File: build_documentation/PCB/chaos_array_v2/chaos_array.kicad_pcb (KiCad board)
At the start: 2 copper layers, 114 x 44 mm, 19 parts, among them SW1 SW_Push, SW2 SW_Push, SW3 OS/Left_Right-hand_Switch, SW4 SW_Push, SW5 SW_Push, U1 RP2040-Zero

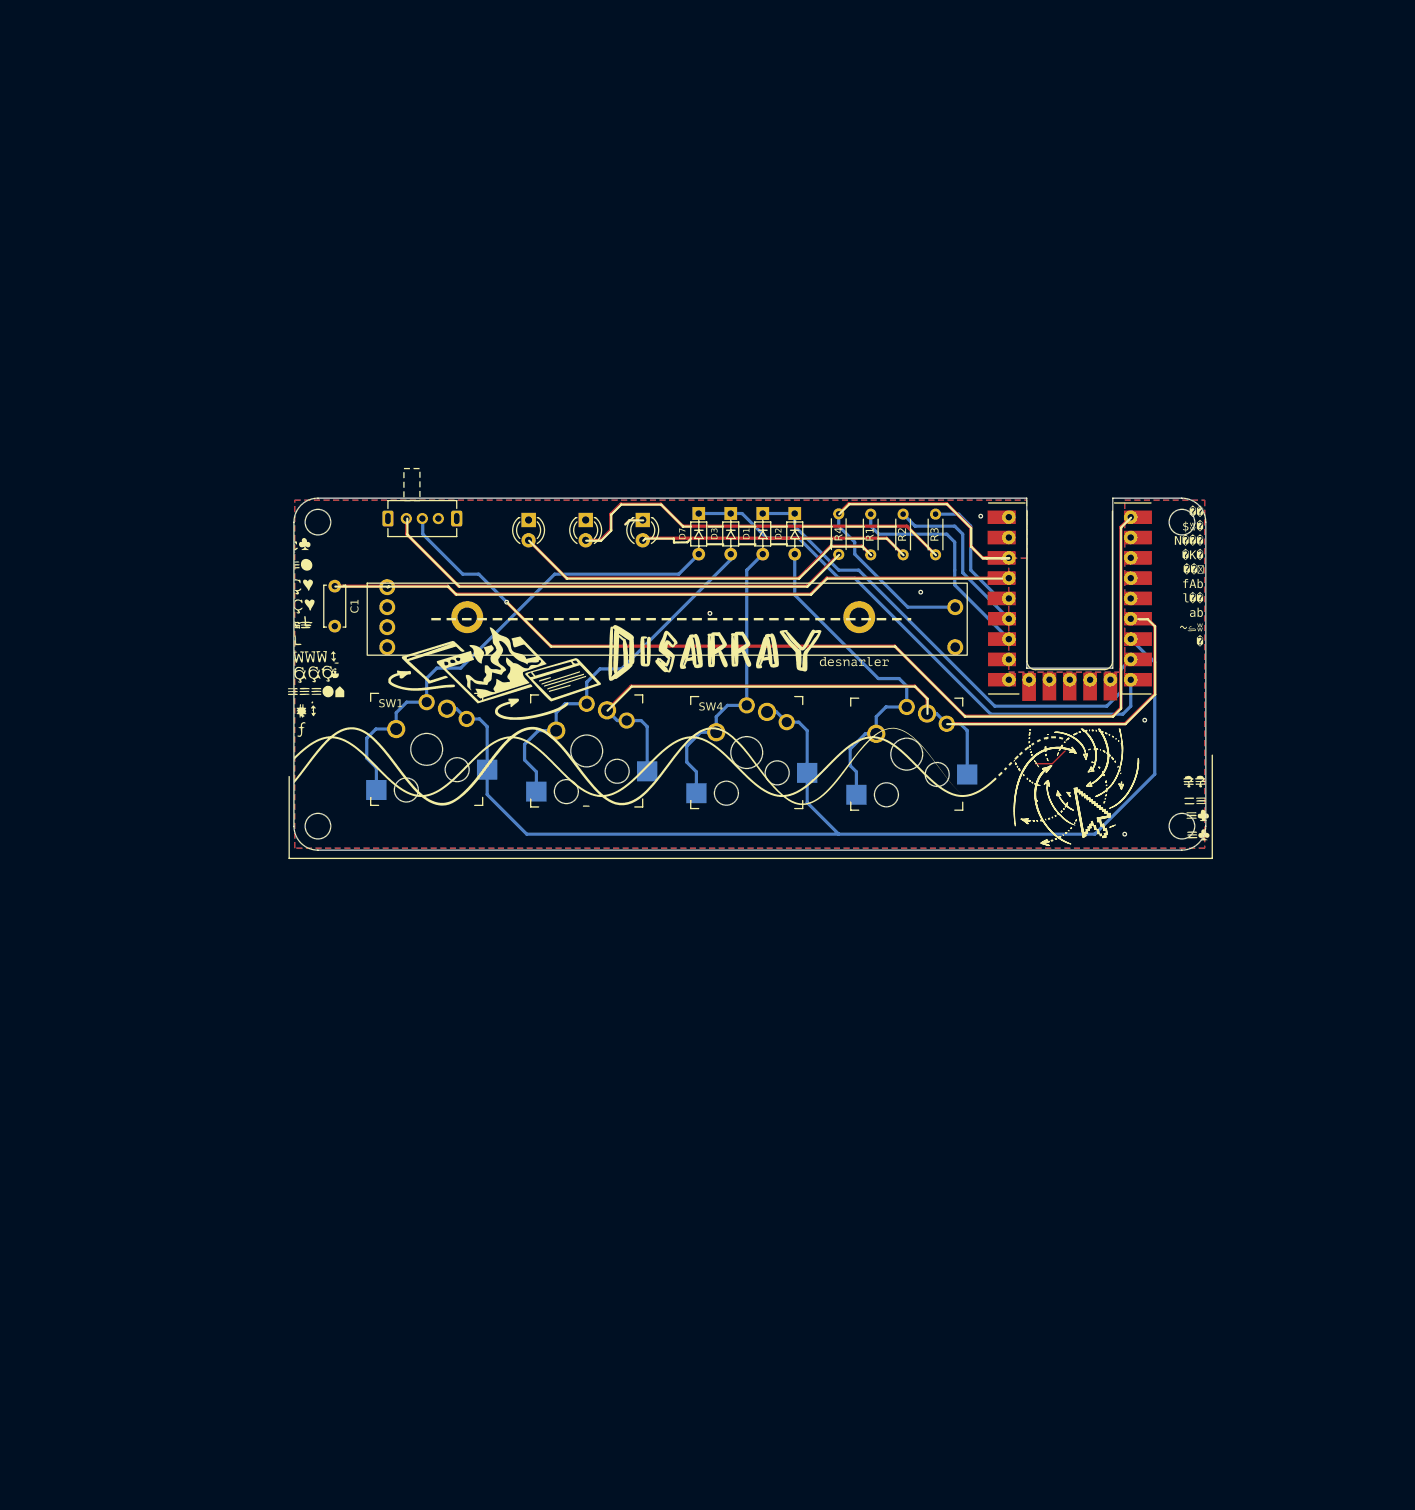
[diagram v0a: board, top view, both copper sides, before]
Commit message: basic layout PCB
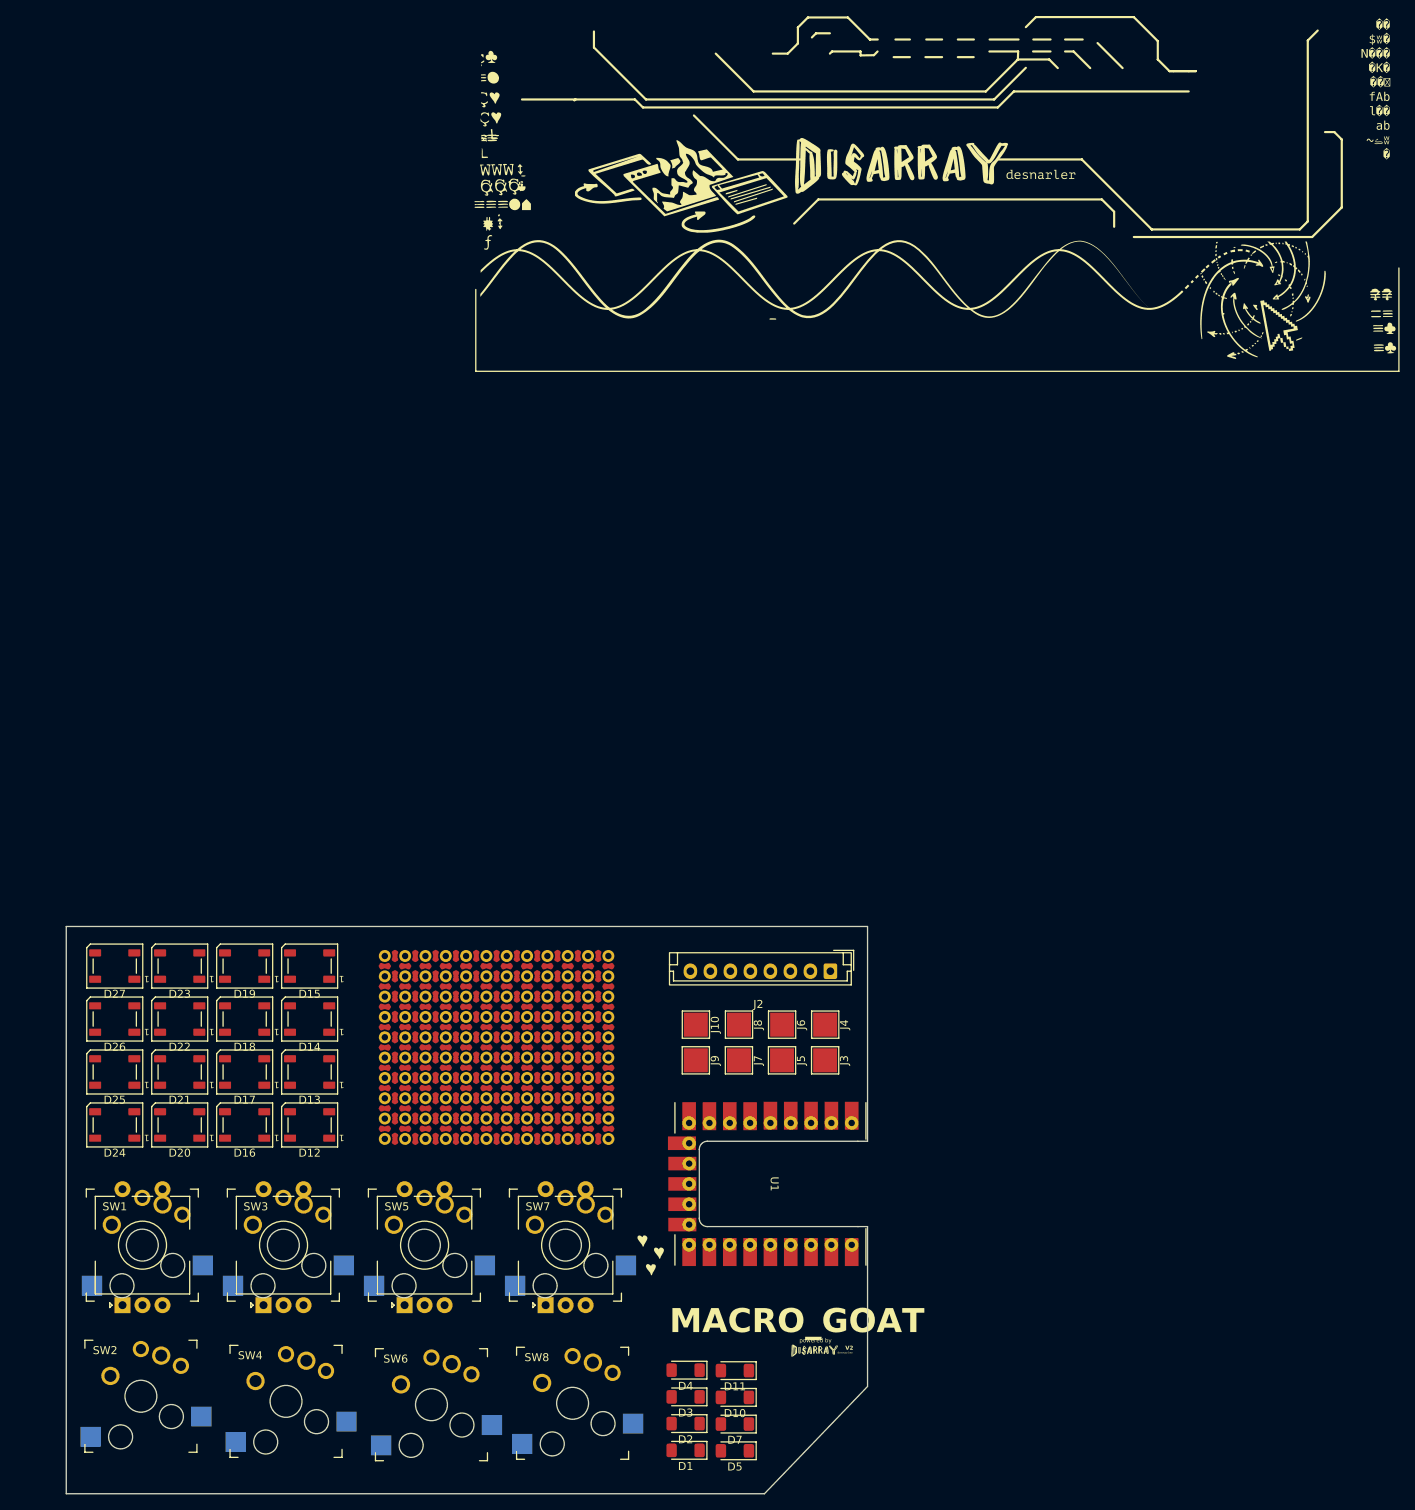
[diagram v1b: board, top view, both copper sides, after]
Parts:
- removed C1: C, Capacitor_THT:C_Disc_D5.0mm_W2.5mm_P5.00mm
- removed D6, D8, D9: LED, LED_THT:LED_D3.0mm
- removed R1, R2, R3: 100R, Resistor_THT:R_Axial_DIN0204_L3.6mm_D1.6mm_P5.08mm_Horizontal
- removed R4: 10k, Resistor_THT:R_Axial_DIN0204_L3.6mm_D1.6mm_P5.08mm_Horizontal
- removed RV1: Analogue_input_slider 10k, CustomFootprints:Potentiometer_slide_75mm_range_60mm_2_sets
- added D10: 1N4148WT, Diode_SMD:D_MiniMELF, F.Cu at (158.0, 150.4)
- added D11: 1N4148WT, Diode_SMD:D_MiniMELF, F.Cu at (158.0, 147.1)
- added D12: WS2812B, LED_SMD:LED_WS2812B_PLCC4_5.0x5.0mm_P3.2mm, F.Cu at (104.9, 116.3)
- added D13: WS2812B, LED_SMD:LED_WS2812B_PLCC4_5.0x5.0mm_P3.2mm, F.Cu at (104.9, 109.7)
- added D14: WS2812B, LED_SMD:LED_WS2812B_PLCC4_5.0x5.0mm_P3.2mm, F.Cu at (104.9, 103.1)
- added D15: WS2812B, LED_SMD:LED_WS2812B_PLCC4_5.0x5.0mm_P3.2mm, F.Cu at (104.9, 96.5)
- added D16: WS2812B, LED_SMD:LED_WS2812B_PLCC4_5.0x5.0mm_P3.2mm, F.Cu at (96.7, 116.3)
- added D17: WS2812B, LED_SMD:LED_WS2812B_PLCC4_5.0x5.0mm_P3.2mm, F.Cu at (96.7, 109.7)
- added D18: WS2812B, LED_SMD:LED_WS2812B_PLCC4_5.0x5.0mm_P3.2mm, F.Cu at (96.7, 103.1)
- added D19: WS2812B, LED_SMD:LED_WS2812B_PLCC4_5.0x5.0mm_P3.2mm, F.Cu at (96.7, 96.5)
- added D20: WS2812B, LED_SMD:LED_WS2812B_PLCC4_5.0x5.0mm_P3.2mm, F.Cu at (88.6, 116.3)
- added D21: WS2812B, LED_SMD:LED_WS2812B_PLCC4_5.0x5.0mm_P3.2mm, F.Cu at (88.6, 109.7)
- added D22: WS2812B, LED_SMD:LED_WS2812B_PLCC4_5.0x5.0mm_P3.2mm, F.Cu at (88.6, 103.1)
- added D23: WS2812B, LED_SMD:LED_WS2812B_PLCC4_5.0x5.0mm_P3.2mm, F.Cu at (88.6, 96.5)
- added D24: WS2812B, LED_SMD:LED_WS2812B_PLCC4_5.0x5.0mm_P3.2mm, F.Cu at (80.5, 116.3)
- added D25: WS2812B, LED_SMD:LED_WS2812B_PLCC4_5.0x5.0mm_P3.2mm, F.Cu at (80.5, 109.7)
- added D26: WS2812B, LED_SMD:LED_WS2812B_PLCC4_5.0x5.0mm_P3.2mm, F.Cu at (80.5, 103.1)
- added D27: WS2812B, LED_SMD:LED_WS2812B_PLCC4_5.0x5.0mm_P3.2mm, F.Cu at (80.5, 96.5)
- added D4: 1N4148WT, Diode_SMD:D_MiniMELF, F.Cu at (151.9, 147.0)
- added D5: 1N4148WT, Diode_SMD:D_MiniMELF, F.Cu at (158.0, 157.1)
- added J10: Conn_01x01_Pin, TestPoint:TestPoint_Pad_3.0x3.0mm, F.Cu at (153.1, 103.8)
- added J2: Conn_01x08_Socket, Connector_JST:JST_EH_B8B-EH-A_1x08_P2.50mm_Vertical, F.Cu at (170.0, 97.1)
- added J3: Conn_01x01_Pin, TestPoint:TestPoint_Pad_3.0x3.0mm, F.Cu at (169.3, 108.3)
- added J4: Conn_01x01_Pin, TestPoint:TestPoint_Pad_3.0x3.0mm, F.Cu at (169.3, 103.8)
- added J5: Conn_01x01_Pin, TestPoint:TestPoint_Pad_3.0x3.0mm, F.Cu at (163.9, 108.3)
- added J6: Conn_01x01_Pin, TestPoint:TestPoint_Pad_3.0x3.0mm, F.Cu at (163.9, 103.8)
- added J7: Conn_01x01_Pin, TestPoint:TestPoint_Pad_3.0x3.0mm, F.Cu at (158.5, 108.3)
- added J8: Conn_01x01_Pin, TestPoint:TestPoint_Pad_3.0x3.0mm, F.Cu at (158.5, 103.8)
- added J9: Conn_01x01_Pin, TestPoint:TestPoint_Pad_3.0x3.0mm, F.Cu at (153.1, 108.3)
- added REF**: PerfBoard_THT_SMD_PAD_BOTTOM, TestPoint:PerfBoard_THT_SMD_PAD_BOTTOM, F.Cu at (142.2, 95.2)
- added REF**: PerfBoard_THT_SMD_PAD_RIGHT, TestPoint:PerfBoard_THT_SMD_PAD_RIGHT, F.Cu at (134.6, 118.1)
- added REF**: PerfBoard_THT_SMD_PAD_BOTTOM, TestPoint:PerfBoard_THT_SMD_PAD_BOTTOM, F.Cu at (142.2, 105.4)
- added REF**: PerfBoard_THT_SMD_PAD_RIGHT, TestPoint:PerfBoard_THT_SMD_PAD_RIGHT, F.Cu at (139.7, 118.1)
- added REF**: PerfBoard_THT_SMD_PAD_BOTTOM, TestPoint:PerfBoard_THT_SMD_PAD_BOTTOM, F.Cu at (142.2, 102.9)
- added REF**: PerfBoard_THT_SMD_PAD_RIGHT, TestPoint:PerfBoard_THT_SMD_PAD_RIGHT, F.Cu at (119.3, 118.1)
- added REF**: PerfBoard_THT_SMD_PAD_BOTTOM, TestPoint:PerfBoard_THT_SMD_PAD_BOTTOM, F.Cu at (142.2, 113.0)
- added REF**: PerfBoard_THT_SMD_PAD_RIGHT, TestPoint:PerfBoard_THT_SMD_PAD_RIGHT, F.Cu at (132.0, 118.1)
- added REF**: PerfBoard_THT_SMD_PAD_BOTTOM, TestPoint:PerfBoard_THT_SMD_PAD_BOTTOM, F.Cu at (142.2, 115.6)
- added REF**: PerfBoard_THT_SMD_PAD_BOTTOM, TestPoint:PerfBoard_THT_SMD_PAD_BOTTOM, F.Cu at (142.2, 97.8)
- added REF**: PerfBoard_THT_SMD_PAD_BOTTOM, TestPoint:PerfBoard_THT_SMD_PAD_BOTTOM, F.Cu at (142.2, 100.3)
- added REF**: PerfBoard_THT_PAD, TestPoint:PerfBoard_THT_PAD, F.Cu at (142.2, 118.1)
- added REF**: PerfBoard_THT_SMD_PAD_RIGHT, TestPoint:PerfBoard_THT_SMD_PAD_RIGHT, F.Cu at (129.5, 118.1)
- added REF**: PerfBoard_THT_SMD_PAD_RIGHT, TestPoint:PerfBoard_THT_SMD_PAD_RIGHT, F.Cu at (116.8, 118.1)
- added REF**: PerfBoard_THT_SMD_PAD_RIGHT, TestPoint:PerfBoard_THT_SMD_PAD_RIGHT, F.Cu at (124.4, 118.1)
- added REF**: PerfBoard_THT_SMD_PAD_RIGHT, TestPoint:PerfBoard_THT_SMD_PAD_RIGHT, F.Cu at (114.3, 118.1)
- added REF**: PerfBoard_THT_SMD_PAD_BOTTOM, TestPoint:PerfBoard_THT_SMD_PAD_BOTTOM, F.Cu at (142.2, 107.9)
- added REF**: PerfBoard_THT_SMD_PAD_BOTTOM, TestPoint:PerfBoard_THT_SMD_PAD_BOTTOM, F.Cu at (142.2, 110.5)
- added REF**: PerfBoard_THT_SMD_PAD_RIGHT, TestPoint:PerfBoard_THT_SMD_PAD_RIGHT, F.Cu at (127.0, 118.1)
- added REF**: PerfBoard_THT_SMD_PAD_RIGHT, TestPoint:PerfBoard_THT_SMD_PAD_RIGHT, F.Cu at (121.9, 118.1)
- added REF**: PerfBoard_THT_SMD_PAD_RIGHT, TestPoint:PerfBoard_THT_SMD_PAD_RIGHT, F.Cu at (137.1, 118.1)
- added REF**100: PerfBoard_THT_SMD_PAD, TestPoint:PerfBoard_THT_SMD_PAD, F.Cu at (116.8, 113.0)
- added REF**101: PerfBoard_THT_SMD_PAD, TestPoint:PerfBoard_THT_SMD_PAD, F.Cu at (119.3, 113.0)
- added REF**102: PerfBoard_THT_SMD_PAD, TestPoint:PerfBoard_THT_SMD_PAD, F.Cu at (121.9, 113.0)
- added REF**103: PerfBoard_THT_SMD_PAD, TestPoint:PerfBoard_THT_SMD_PAD, F.Cu at (124.4, 113.0)
- added REF**104: PerfBoard_THT_SMD_PAD, TestPoint:PerfBoard_THT_SMD_PAD, F.Cu at (127.0, 113.0)
- added REF**105: PerfBoard_THT_SMD_PAD, TestPoint:PerfBoard_THT_SMD_PAD, F.Cu at (129.5, 113.0)
- added REF**106: PerfBoard_THT_SMD_PAD, TestPoint:PerfBoard_THT_SMD_PAD, F.Cu at (132.0, 113.0)
- added REF**107: PerfBoard_THT_SMD_PAD, TestPoint:PerfBoard_THT_SMD_PAD, F.Cu at (134.6, 113.0)
- added REF**108: PerfBoard_THT_SMD_PAD, TestPoint:PerfBoard_THT_SMD_PAD, F.Cu at (137.1, 113.0)
- added REF**109: PerfBoard_THT_SMD_PAD, TestPoint:PerfBoard_THT_SMD_PAD, F.Cu at (139.7, 113.0)
- added REF**110: PerfBoard_THT_SMD_PAD, TestPoint:PerfBoard_THT_SMD_PAD, F.Cu at (114.3, 115.5)
- added REF**111: PerfBoard_THT_SMD_PAD, TestPoint:PerfBoard_THT_SMD_PAD, F.Cu at (116.8, 115.5)
- added REF**112: PerfBoard_THT_SMD_PAD, TestPoint:PerfBoard_THT_SMD_PAD, F.Cu at (119.3, 115.5)
- added REF**113: PerfBoard_THT_SMD_PAD, TestPoint:PerfBoard_THT_SMD_PAD, F.Cu at (121.9, 115.5)
- added REF**114: PerfBoard_THT_SMD_PAD, TestPoint:PerfBoard_THT_SMD_PAD, F.Cu at (124.4, 115.5)
- added REF**115: PerfBoard_THT_SMD_PAD, TestPoint:PerfBoard_THT_SMD_PAD, F.Cu at (127.0, 115.5)
- added REF**116: PerfBoard_THT_SMD_PAD, TestPoint:PerfBoard_THT_SMD_PAD, F.Cu at (129.5, 115.5)
- added REF**117: PerfBoard_THT_SMD_PAD, TestPoint:PerfBoard_THT_SMD_PAD, F.Cu at (132.0, 115.5)
- added REF**118: PerfBoard_THT_SMD_PAD, TestPoint:PerfBoard_THT_SMD_PAD, F.Cu at (134.6, 115.5)
- added REF**119: PerfBoard_THT_SMD_PAD, TestPoint:PerfBoard_THT_SMD_PAD, F.Cu at (137.1, 115.5)
- added REF**120: PerfBoard_THT_SMD_PAD, TestPoint:PerfBoard_THT_SMD_PAD, F.Cu at (139.7, 115.5)
- added REF**22: PerfBoard_THT_SMD_PAD, TestPoint:PerfBoard_THT_SMD_PAD, F.Cu at (114.3, 95.2)
- added REF**23: PerfBoard_THT_SMD_PAD, TestPoint:PerfBoard_THT_SMD_PAD, F.Cu at (116.8, 95.2)
- added REF**24: PerfBoard_THT_SMD_PAD, TestPoint:PerfBoard_THT_SMD_PAD, F.Cu at (119.3, 95.2)
- added REF**25: PerfBoard_THT_SMD_PAD, TestPoint:PerfBoard_THT_SMD_PAD, F.Cu at (121.9, 95.2)
- added REF**26: PerfBoard_THT_SMD_PAD, TestPoint:PerfBoard_THT_SMD_PAD, F.Cu at (124.4, 95.2)
- added REF**27: PerfBoard_THT_SMD_PAD, TestPoint:PerfBoard_THT_SMD_PAD, F.Cu at (127.0, 95.2)
- added REF**28: PerfBoard_THT_SMD_PAD, TestPoint:PerfBoard_THT_SMD_PAD, F.Cu at (129.5, 95.2)
- added REF**29: PerfBoard_THT_SMD_PAD, TestPoint:PerfBoard_THT_SMD_PAD, F.Cu at (132.0, 95.2)
- added REF**30: PerfBoard_THT_SMD_PAD, TestPoint:PerfBoard_THT_SMD_PAD, F.Cu at (134.6, 95.2)
- added REF**31: PerfBoard_THT_SMD_PAD, TestPoint:PerfBoard_THT_SMD_PAD, F.Cu at (137.1, 95.2)
- added REF**32: PerfBoard_THT_SMD_PAD, TestPoint:PerfBoard_THT_SMD_PAD, F.Cu at (139.7, 95.2)
- added REF**33: PerfBoard_THT_SMD_PAD, TestPoint:PerfBoard_THT_SMD_PAD, F.Cu at (114.3, 97.8)
- added REF**34: PerfBoard_THT_SMD_PAD, TestPoint:PerfBoard_THT_SMD_PAD, F.Cu at (116.8, 97.8)
- added REF**35: PerfBoard_THT_SMD_PAD, TestPoint:PerfBoard_THT_SMD_PAD, F.Cu at (119.3, 97.8)
- added REF**36: PerfBoard_THT_SMD_PAD, TestPoint:PerfBoard_THT_SMD_PAD, F.Cu at (121.9, 97.8)
- added REF**37: PerfBoard_THT_SMD_PAD, TestPoint:PerfBoard_THT_SMD_PAD, F.Cu at (124.4, 97.8)
- added REF**38: PerfBoard_THT_SMD_PAD, TestPoint:PerfBoard_THT_SMD_PAD, F.Cu at (127.0, 97.8)
- added REF**39: PerfBoard_THT_SMD_PAD, TestPoint:PerfBoard_THT_SMD_PAD, F.Cu at (129.5, 97.8)
- added REF**40: PerfBoard_THT_SMD_PAD, TestPoint:PerfBoard_THT_SMD_PAD, F.Cu at (132.0, 97.8)
- added REF**41: PerfBoard_THT_SMD_PAD, TestPoint:PerfBoard_THT_SMD_PAD, F.Cu at (134.6, 97.8)
- added REF**42: PerfBoard_THT_SMD_PAD, TestPoint:PerfBoard_THT_SMD_PAD, F.Cu at (137.1, 97.8)
- added REF**43: PerfBoard_THT_SMD_PAD, TestPoint:PerfBoard_THT_SMD_PAD, F.Cu at (139.7, 97.8)
- added REF**44: PerfBoard_THT_SMD_PAD, TestPoint:PerfBoard_THT_SMD_PAD, F.Cu at (114.3, 100.3)
- added REF**45: PerfBoard_THT_SMD_PAD, TestPoint:PerfBoard_THT_SMD_PAD, F.Cu at (116.8, 100.3)
- added REF**46: PerfBoard_THT_SMD_PAD, TestPoint:PerfBoard_THT_SMD_PAD, F.Cu at (119.3, 100.3)
- added REF**47: PerfBoard_THT_SMD_PAD, TestPoint:PerfBoard_THT_SMD_PAD, F.Cu at (121.9, 100.3)
- added REF**48: PerfBoard_THT_SMD_PAD, TestPoint:PerfBoard_THT_SMD_PAD, F.Cu at (124.4, 100.3)
- added REF**49: PerfBoard_THT_SMD_PAD, TestPoint:PerfBoard_THT_SMD_PAD, F.Cu at (127.0, 100.3)
- added REF**50: PerfBoard_THT_SMD_PAD, TestPoint:PerfBoard_THT_SMD_PAD, F.Cu at (129.5, 100.3)
- added REF**51: PerfBoard_THT_SMD_PAD, TestPoint:PerfBoard_THT_SMD_PAD, F.Cu at (132.0, 100.3)
- added REF**52: PerfBoard_THT_SMD_PAD, TestPoint:PerfBoard_THT_SMD_PAD, F.Cu at (134.6, 100.3)
- added REF**53: PerfBoard_THT_SMD_PAD, TestPoint:PerfBoard_THT_SMD_PAD, F.Cu at (137.1, 100.3)
- added REF**54: PerfBoard_THT_SMD_PAD, TestPoint:PerfBoard_THT_SMD_PAD, F.Cu at (139.7, 100.3)
- added REF**55: PerfBoard_THT_SMD_PAD, TestPoint:PerfBoard_THT_SMD_PAD, F.Cu at (114.3, 102.8)
- added REF**56: PerfBoard_THT_SMD_PAD, TestPoint:PerfBoard_THT_SMD_PAD, F.Cu at (116.8, 102.8)
- added REF**57: PerfBoard_THT_SMD_PAD, TestPoint:PerfBoard_THT_SMD_PAD, F.Cu at (119.3, 102.8)
- added REF**58: PerfBoard_THT_SMD_PAD, TestPoint:PerfBoard_THT_SMD_PAD, F.Cu at (121.9, 102.8)
- added REF**59: PerfBoard_THT_SMD_PAD, TestPoint:PerfBoard_THT_SMD_PAD, F.Cu at (124.4, 102.8)
- added REF**60: PerfBoard_THT_SMD_PAD, TestPoint:PerfBoard_THT_SMD_PAD, F.Cu at (127.0, 102.8)
- added REF**61: PerfBoard_THT_SMD_PAD, TestPoint:PerfBoard_THT_SMD_PAD, F.Cu at (129.5, 102.8)
- added REF**62: PerfBoard_THT_SMD_PAD, TestPoint:PerfBoard_THT_SMD_PAD, F.Cu at (132.0, 102.8)
- added REF**63: PerfBoard_THT_SMD_PAD, TestPoint:PerfBoard_THT_SMD_PAD, F.Cu at (134.6, 102.8)
- added REF**64: PerfBoard_THT_SMD_PAD, TestPoint:PerfBoard_THT_SMD_PAD, F.Cu at (137.1, 102.8)
- added REF**65: PerfBoard_THT_SMD_PAD, TestPoint:PerfBoard_THT_SMD_PAD, F.Cu at (139.7, 102.8)
- added REF**66: PerfBoard_THT_SMD_PAD, TestPoint:PerfBoard_THT_SMD_PAD, F.Cu at (114.3, 105.4)
- added REF**67: PerfBoard_THT_SMD_PAD, TestPoint:PerfBoard_THT_SMD_PAD, F.Cu at (116.8, 105.4)
- added REF**68: PerfBoard_THT_SMD_PAD, TestPoint:PerfBoard_THT_SMD_PAD, F.Cu at (119.3, 105.4)
- added REF**69: PerfBoard_THT_SMD_PAD, TestPoint:PerfBoard_THT_SMD_PAD, F.Cu at (121.9, 105.4)
- added REF**70: PerfBoard_THT_SMD_PAD, TestPoint:PerfBoard_THT_SMD_PAD, F.Cu at (124.4, 105.4)
- added REF**71: PerfBoard_THT_SMD_PAD, TestPoint:PerfBoard_THT_SMD_PAD, F.Cu at (127.0, 105.4)
- added REF**72: PerfBoard_THT_SMD_PAD, TestPoint:PerfBoard_THT_SMD_PAD, F.Cu at (129.5, 105.4)
- added REF**73: PerfBoard_THT_SMD_PAD, TestPoint:PerfBoard_THT_SMD_PAD, F.Cu at (132.0, 105.4)
- added REF**74: PerfBoard_THT_SMD_PAD, TestPoint:PerfBoard_THT_SMD_PAD, F.Cu at (134.6, 105.4)
- added REF**75: PerfBoard_THT_SMD_PAD, TestPoint:PerfBoard_THT_SMD_PAD, F.Cu at (137.1, 105.4)
- added REF**76: PerfBoard_THT_SMD_PAD, TestPoint:PerfBoard_THT_SMD_PAD, F.Cu at (139.7, 105.4)
- added REF**77: PerfBoard_THT_SMD_PAD, TestPoint:PerfBoard_THT_SMD_PAD, F.Cu at (114.3, 107.9)
- added REF**78: PerfBoard_THT_SMD_PAD, TestPoint:PerfBoard_THT_SMD_PAD, F.Cu at (116.8, 107.9)
- added REF**79: PerfBoard_THT_SMD_PAD, TestPoint:PerfBoard_THT_SMD_PAD, F.Cu at (119.3, 107.9)
- added REF**80: PerfBoard_THT_SMD_PAD, TestPoint:PerfBoard_THT_SMD_PAD, F.Cu at (121.9, 107.9)
- added REF**81: PerfBoard_THT_SMD_PAD, TestPoint:PerfBoard_THT_SMD_PAD, F.Cu at (124.4, 107.9)
- added REF**82: PerfBoard_THT_SMD_PAD, TestPoint:PerfBoard_THT_SMD_PAD, F.Cu at (127.0, 107.9)
- added REF**83: PerfBoard_THT_SMD_PAD, TestPoint:PerfBoard_THT_SMD_PAD, F.Cu at (129.5, 107.9)
- added REF**84: PerfBoard_THT_SMD_PAD, TestPoint:PerfBoard_THT_SMD_PAD, F.Cu at (132.0, 107.9)
- added REF**85: PerfBoard_THT_SMD_PAD, TestPoint:PerfBoard_THT_SMD_PAD, F.Cu at (134.6, 107.9)
- added REF**86: PerfBoard_THT_SMD_PAD, TestPoint:PerfBoard_THT_SMD_PAD, F.Cu at (137.1, 107.9)
- added REF**87: PerfBoard_THT_SMD_PAD, TestPoint:PerfBoard_THT_SMD_PAD, F.Cu at (139.7, 107.9)
- added REF**88: PerfBoard_THT_SMD_PAD, TestPoint:PerfBoard_THT_SMD_PAD, F.Cu at (114.3, 110.5)
- added REF**89: PerfBoard_THT_SMD_PAD, TestPoint:PerfBoard_THT_SMD_PAD, F.Cu at (116.8, 110.5)
- added REF**90: PerfBoard_THT_SMD_PAD, TestPoint:PerfBoard_THT_SMD_PAD, F.Cu at (119.3, 110.5)
- added REF**91: PerfBoard_THT_SMD_PAD, TestPoint:PerfBoard_THT_SMD_PAD, F.Cu at (121.9, 110.5)
- added REF**92: PerfBoard_THT_SMD_PAD, TestPoint:PerfBoard_THT_SMD_PAD, F.Cu at (124.4, 110.5)
- added REF**93: PerfBoard_THT_SMD_PAD, TestPoint:PerfBoard_THT_SMD_PAD, F.Cu at (127.0, 110.5)
- added REF**94: PerfBoard_THT_SMD_PAD, TestPoint:PerfBoard_THT_SMD_PAD, F.Cu at (129.5, 110.5)
- added REF**95: PerfBoard_THT_SMD_PAD, TestPoint:PerfBoard_THT_SMD_PAD, F.Cu at (132.0, 110.5)
- added REF**96: PerfBoard_THT_SMD_PAD, TestPoint:PerfBoard_THT_SMD_PAD, F.Cu at (134.6, 110.5)
- added REF**97: PerfBoard_THT_SMD_PAD, TestPoint:PerfBoard_THT_SMD_PAD, F.Cu at (137.1, 110.5)
- added REF**98: PerfBoard_THT_SMD_PAD, TestPoint:PerfBoard_THT_SMD_PAD, F.Cu at (139.7, 110.5)
- added REF**99: PerfBoard_THT_SMD_PAD, TestPoint:PerfBoard_THT_SMD_PAD, F.Cu at (114.3, 113.0)
- added SW6: SW_Push, footprints:Kailh_socket_MX_PG1350_optional, F.Cu at (120.1, 151.3)
- added SW7: RotaryEncoder_Switch, footprints:Kailh_socket_MX_PG1350_EC11_optional, F.Cu at (136.8, 131.4)
- added SW8: SW_Push, footprints:Kailh_socket_MX_PG1350_optional, F.Cu at (137.7, 151.1)
- D1, D2, D3, D7: footprint Key_Switches:D_DO-35_SOD27_P5.08mm_Horizontal -> Diode_SMD:D_MiniMELF
- SW1, SW5: value SW_Push -> RotaryEncoder_Switch; footprint Key_Switches:Kailh_socket_MX_PG1350_optional -> footprints:Kailh_socket_MX_PG1350_EC11_optional
- SW2, SW4: footprint Key_Switches:Kailh_socket_MX_PG1350_optional -> footprints:Kailh_socket_MX_PG1350_optional
- SW3: value OS/Left_Right-hand_Switch -> RotaryEncoder_Switch; footprint CustomFootprints:SPDT_3pin_2_pos_1P2T_tht_2.54mm_switch_sk12d07 -> footprints:Kailh_socket_MX_PG1350_EC11_optional
- U1: footprint CustomFootprints:RP2040 Zero -> RP2040 Zero:RP2040 Zero
- moved D1 118.8 mm to (151.9, 157.0), turned to 180 degrees
- moved D2 115.8 mm to (151.9, 153.7), turned to 180 degrees
- moved D7 115.2 mm to (158.0, 153.7), turned to 180 degrees
- moved D3 111.8 mm to (151.9, 150.3), turned to 180 degrees
- moved SW4 99.5 mm to (101.9, 150.9)
- moved SW2 98.0 mm to (83.8, 150.3)
- moved SW3 94.0 mm to (101.6, 131.4)
- moved SW5 86.0 mm to (119.2, 131.4)
- moved SW1 71.4 mm to (83.9, 131.4)
- moved U1 64.2 mm to (149.6, 113.6), turned to -90 degrees
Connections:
- D1 pad 1: Net-(D1-K) -> /row_1
- D2 pad 1: Net-(D1-K) -> /row_1
- D3 pad 1: Net-(D3-K) -> /row_1
- D7 pad 1: Net-(D3-K) -> /row_0
- SW2 pad 1: Net-(U1-GP5) -> /col_0
- SW2 pad 2: Net-(D3-A) -> Net-(D1-A)
- SW4 pad 1: Net-(U1-GP6) -> /col_1
- SW4 pad 2: Net-(D1-A) -> Net-(D2-A)
- U1 pad 1: unconnected-(U1-5V-Pad1) -> +5V
- U1 pad 10: Net-(SW3-B) -> /col_0
- U1 pad 11: unconnected-(U1-GP1-Pad11)_1 -> /col_1
- U1 pad 12: unconnected-(U1-GP2-Pad12) -> /col_2
- U1 pad 13: unconnected-(U1-GP3-Pad13)_1 -> /col_3
- U1 pad 15: Net-(U1-GP5) -> unconnected-(U1-GP5-Pad15)_1
- U1 pad 16: Net-(U1-GP6) -> unconnected-(U1-GP6-Pad16)
- U1 pad 17: Net-(D1-K) -> /row_0
- U1 pad 18: Net-(D3-K) -> /row_1
- U1 pad 19: unconnected-(U1-GP13-Pad19) -> /LED_out
- U1 pad 22: unconnected-(U1-GP10-Pad22) -> /enc_b
- U1 pad 23: unconnected-(U1-GP9-Pad23)_1 -> /enc_a
- U1 pad 3: Net-(U1-3V3) -> +3.3V
- U1 pad 4: Net-(U1-GP29) -> unconnected-(U1-GP29-Pad4)
- U1 pad 5: Net-(U1-GP28) -> /gp28
- U1 pad 6: Net-(U1-GP27) -> /gp27
- U1 pad 7: Net-(U1-GP26) -> /gp26
- U1 pad 8: unconnected-(U1-GP15-Pad8) -> /gp15
- U1 pad 9: unconnected-(U1-GP14-Pad9) -> /gp14
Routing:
- net Net-(U1-GP6): track 141.8 -> 0.00 mm
- net Net-(SW3-B): track 123.5 -> 0.00 mm, vias 1 -> 0
- net Net-(U1-GP5): track 105.1 -> 0.00 mm
- net Net-(U1-GP29): track 84.7 -> 0.00 mm
- net Net-(D3-K): track 68.1 -> 0.00 mm
- net Net-(D7-A): track 61.2 -> 0.00 mm
- net Net-(D1-K): track 61.0 -> 0.00 mm
- net Net-(SW3-C): track 60.3 -> 0.00 mm
- net Net-(D9-A): track 49.4 -> 0.00 mm
- net Net-(U1-3V3): track 48.0 -> 0.00 mm
- net Net-(D6-A): track 46.8 -> 0.00 mm
- net Net-(D3-A): track 45.7 -> 0.00 mm
- net Net-(D2-A): track 43.2 -> 0.00 mm
- net Net-(D1-A): track 37.1 -> 0.00 mm
- net Net-(D8-A): track 33.5 -> 0.00 mm
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- removed copper zone on B.Cu, net GND
- removed copper zone on F.Cu, net GND
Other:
- board size 114 x 44 mm -> 100.2 x 70.9 mm
- board text added: "MACRO_GOAT"
- board text added: "V2"
- board text added: "powered by"
- board text removed: "+"
- board text removed: "-"

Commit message: Routing
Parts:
- added C1: C_Polarized, Capacitor_SMD:CP_Elec_6.3x5.8, F.Cu at (114.3, 115.3)
- added REF**22: PerfBoard_THT_SMD_PAD, TestPoint:PerfBoard_THT_SMD_PAD, F.Cu at (111.8, 95.6)
- added REF**23: PerfBoard_THT_SMD_PAD, TestPoint:PerfBoard_THT_SMD_PAD, F.Cu at (114.3, 95.6)
- added REF**24: PerfBoard_THT_SMD_PAD, TestPoint:PerfBoard_THT_SMD_PAD, F.Cu at (116.9, 95.6)
- added REF**33: PerfBoard_THT_SMD_PAD, TestPoint:PerfBoard_THT_SMD_PAD, F.Cu at (111.8, 98.2)
- added REF**34: PerfBoard_THT_SMD_PAD, TestPoint:PerfBoard_THT_SMD_PAD, F.Cu at (114.3, 98.2)
- added REF**35: PerfBoard_THT_SMD_PAD, TestPoint:PerfBoard_THT_SMD_PAD, F.Cu at (116.9, 98.2)
- added REF**44: PerfBoard_THT_SMD_PAD, TestPoint:PerfBoard_THT_SMD_PAD, F.Cu at (111.8, 100.7)
- added REF**45: PerfBoard_THT_SMD_PAD, TestPoint:PerfBoard_THT_SMD_PAD, F.Cu at (114.3, 100.7)
- added REF**46: PerfBoard_THT_SMD_PAD, TestPoint:PerfBoard_THT_SMD_PAD, F.Cu at (116.9, 100.7)
- added REF**55: PerfBoard_THT_SMD_PAD, TestPoint:PerfBoard_THT_SMD_PAD, F.Cu at (111.8, 103.2)
- added REF**56: PerfBoard_THT_SMD_PAD, TestPoint:PerfBoard_THT_SMD_PAD, F.Cu at (114.3, 103.2)
- added REF**57: PerfBoard_THT_SMD_PAD, TestPoint:PerfBoard_THT_SMD_PAD, F.Cu at (116.9, 103.2)
- added REF**66: PerfBoard_THT_SMD_PAD, TestPoint:PerfBoard_THT_SMD_PAD, F.Cu at (111.8, 105.8)
- added REF**67: PerfBoard_THT_SMD_PAD, TestPoint:PerfBoard_THT_SMD_PAD, F.Cu at (114.3, 105.8)
- added REF**68: PerfBoard_THT_SMD_PAD, TestPoint:PerfBoard_THT_SMD_PAD, F.Cu at (116.9, 105.8)
- added REF**77: PerfBoard_THT_SMD_PAD, TestPoint:PerfBoard_THT_SMD_PAD, F.Cu at (111.8, 108.3)
- added REF**78: PerfBoard_THT_SMD_PAD, TestPoint:PerfBoard_THT_SMD_PAD, F.Cu at (114.3, 108.3)
- added REF**79: PerfBoard_THT_SMD_PAD, TestPoint:PerfBoard_THT_SMD_PAD, F.Cu at (116.9, 108.3)
- moved D27 32.4 mm to (105.7, 116.7)
- moved D12 30.4 mm to (81.5, 96.9)
- moved D26 21.9 mm to (97.6, 116.7)
- moved D23 21.8 mm to (105.7, 110.0)
- moved D13 19.9 mm to (89.6, 96.9)
- moved D16 19.9 mm to (81.5, 103.5)
- moved D19 11.4 mm to (105.7, 103.5)
- moved D22 11.4 mm to (97.6, 110.1)
- moved D25 11.4 mm to (89.5, 116.7)
- moved D5 11.4 mm to (158.6, 145.7)
- moved D17 9.53 mm to (89.5, 103.5)
- moved D14 9.52 mm to (97.6, 96.9)
- moved D20 9.43 mm to (81.5, 110.1)
- moved D7 7.69 mm to (151.6, 149.5)
- moved D3 6.79 mm to (151.8, 157.1)
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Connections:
- D12 pad 2: unconnected-(D12-DOUT-Pad2) -> Net-(D12-DOUT)
- D13 pad 2: unconnected-(D13-DOUT-Pad2) -> Net-(D13-DOUT)
- D13 pad 4: unconnected-(D13-DIN-Pad4) -> Net-(D12-DOUT)
- D14 pad 2: unconnected-(D14-DOUT-Pad2) -> Net-(D14-DOUT)
- D14 pad 4: unconnected-(D14-DIN-Pad4) -> Net-(D13-DOUT)
- D15 pad 2: unconnected-(D15-DOUT-Pad2) -> Net-(D15-DOUT)
- D15 pad 4: unconnected-(D15-DIN-Pad4) -> Net-(D14-DOUT)
- D16 pad 2: unconnected-(D16-DOUT-Pad2) -> Net-(D16-DOUT)
- D16 pad 4: unconnected-(D16-DIN-Pad4) -> Net-(D15-DOUT)
- D17 pad 2: unconnected-(D17-DOUT-Pad2) -> Net-(D17-DOUT)
- D17 pad 4: unconnected-(D17-DIN-Pad4) -> Net-(D16-DOUT)
- D18 pad 2: unconnected-(D18-DOUT-Pad2) -> Net-(D18-DOUT)
- D18 pad 4: unconnected-(D18-DIN-Pad4) -> Net-(D17-DOUT)
- D19 pad 4: unconnected-(D19-DIN-Pad4) -> Net-(D18-DOUT)
- D20 pad 2: unconnected-(D20-DOUT-Pad2) -> Net-(D20-DOUT)
- D21 pad 2: unconnected-(D21-DOUT-Pad2) -> Net-(D21-DOUT)
- D21 pad 4: unconnected-(D21-DIN-Pad4) -> Net-(D20-DOUT)
- D22 pad 2: unconnected-(D22-DOUT-Pad2) -> Net-(D22-DOUT)
- D22 pad 4: unconnected-(D22-DIN-Pad4) -> Net-(D21-DOUT)
- D23 pad 2: unconnected-(D23-DOUT-Pad2) -> Net-(D23-DOUT)
- D23 pad 4: unconnected-(D23-DIN-Pad4) -> Net-(D22-DOUT)
- D24 pad 2: unconnected-(D24-DOUT-Pad2) -> Net-(D24-DOUT)
- D24 pad 4: unconnected-(D24-DIN-Pad4) -> Net-(D23-DOUT)
- D25 pad 2: unconnected-(D25-DOUT-Pad2) -> Net-(D25-DOUT)
- D25 pad 4: unconnected-(D25-DIN-Pad4) -> Net-(D24-DOUT)
- D26 pad 2: unconnected-(D26-DOUT-Pad2) -> Net-(D26-DOUT)
- D26 pad 4: unconnected-(D26-DIN-Pad4) -> Net-(D25-DOUT)
- D27 pad 4: unconnected-(D27-DIN-Pad4) -> Net-(D26-DOUT)
- J2 pad 5: /gp14 -> /gp26
- J2 pad 7: /gp26 -> /gp14
- J7 pad 1: /gp14 -> /gp26
- J9 pad 1: /gp26 -> /gp14
- SW3 pad A: /enc_a -> /enc_c
- SW3 pad B: /enc_b -> /enc_d
- SW5 pad A: /enc_a -> /enc_e
- SW5 pad B: /enc_b -> /enc_f
- SW5 pad S2: /col_0 -> /col_2
- SW6 pad 1: /col_0 -> /col_2
- SW7 pad A: /enc_a -> /enc_g
- SW7 pad B: /enc_b -> /enc_h
- SW7 pad S2: /col_1 -> /col_3
- SW8 pad 1: /col_1 -> /col_3
- U1 pad 10: /col_0 -> /row_1
- U1 pad 11: /col_1 -> /row_0
- U1 pad 12: /col_2 -> /col_0
- U1 pad 13: /col_3 -> /col_1
- U1 pad 14: unconnected-(U1-GP4-Pad14) -> /col_2
- U1 pad 15: unconnected-(U1-GP5-Pad15)_1 -> /col_3
- U1 pad 16: unconnected-(U1-GP6-Pad16) -> /enc_g
- U1 pad 17: /row_0 -> /enc_h
- U1 pad 18: /row_1 -> /enc_e
- U1 pad 19: /LED_out -> /enc_b
- U1 pad 20: unconnected-(U1-GP12-Pad20) -> /enc_a
- U1 pad 21: unconnected-(U1-GP11-Pad21) -> /enc_d
- U1 pad 22: /enc_b -> /enc_c
- U1 pad 23: /enc_a -> /enc_f
- U1 pad 4: unconnected-(U1-GP29-Pad4) -> /LED_out
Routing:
- net +5V: track 0.00 -> 261.8 mm
- net /col_0: track 0.00 -> 144.2 mm
- net /col_1: track 0.00 -> 125.1 mm
- net /LED_out: track 0.00 -> 109.2 mm, vias 0 -> 1
- net /col_2: track 0.00 -> 89.8 mm
- net Net-(D1-A): track 0.00 -> 87.2 mm
- net Net-(D7-A): track 0.00 -> 85.3 mm
- net Net-(D10-A): track 0.00 -> 74.7 mm
- net Net-(D2-A): track 0.00 -> 74.2 mm
- net /enc_b: track 0.00 -> 72.1 mm
- net /enc_a: track 0.00 -> 67.0 mm
- net /col_3: track 0.00 -> 63.5 mm
- net /enc_d: track 0.00 -> 55.0 mm
- net /enc_c: track 0.00 -> 50.3 mm
- net Net-(D11-A): track 0.00 -> 48.5 mm
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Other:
- outline, holes or cut-outs redrawn

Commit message: PCE reassemble switches
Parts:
- moved D12 4.70 mm to (76.8, 96.9)
- moved D13 4.70 mm to (84.9, 96.9)
- moved D14 4.70 mm to (92.9, 96.9)
- moved D15 4.70 mm to (101.0, 96.9)
- moved D16 4.70 mm to (76.8, 103.5)
- moved D17 4.70 mm to (84.8, 103.5)
- moved D18 4.70 mm to (92.9, 103.5)
- moved D19 4.70 mm to (101.0, 103.5)
- moved D20 4.70 mm to (76.8, 110.1)
- moved D21 4.70 mm to (84.8, 110.1)
- moved D22 4.70 mm to (92.9, 110.1)
- moved D23 4.70 mm to (101.0, 110.0)
- moved D24 4.70 mm to (76.8, 116.7)
- moved D25 4.70 mm to (84.8, 116.7)
- moved D26 4.70 mm to (92.9, 116.7)
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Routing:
- net +5V: track 261.8 -> 324.6 mm
- net Net-(D23-DOUT): track 34.4 -> 0.00 mm
- net GND: track 0.98 -> 18.0 mm
- net Net-(D26-DOUT): track 5.79 -> 0.00 mm
- net Net-(D25-DOUT): track 5.79 -> 0.00 mm
- net Net-(D24-DOUT): track 5.79 -> 0.00 mm
- net Net-(D22-DOUT): track 5.79 -> 0.00 mm
- net Net-(D21-DOUT): track 5.79 -> 0.00 mm
- net Net-(D20-DOUT): track 5.79 -> 0.00 mm
- net Net-(D18-DOUT): track 5.79 -> 0.00 mm
- net Net-(D17-DOUT): track 5.79 -> 0.00 mm
- net Net-(D16-DOUT): track 5.79 -> 0.00 mm
- net Net-(D14-DOUT): track 5.79 -> 0.00 mm
- net Net-(D13-DOUT): track 5.79 -> 0.00 mm
- net Net-(D12-DOUT): track 5.79 -> 0.00 mm
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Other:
- board size 100.2 x 70.9 mm -> 106.4 x 70.9 mm
- board text added: "3.3v"
- board text added: "5v"
- board text added: "GND"
- board text added: "GP14"
- board text added: "GP15"
- board text added: "GP26"
- board text added: "GP27"
- board text added: "GP28"
